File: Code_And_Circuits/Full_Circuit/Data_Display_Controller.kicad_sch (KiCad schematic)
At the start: 24 parts, among them M2 Stepper_Motor_bipolar, SW2 SW_Push_Dual_JST_XH_Input, U2 L293D, U5 TXB0104D, U6 74HC595

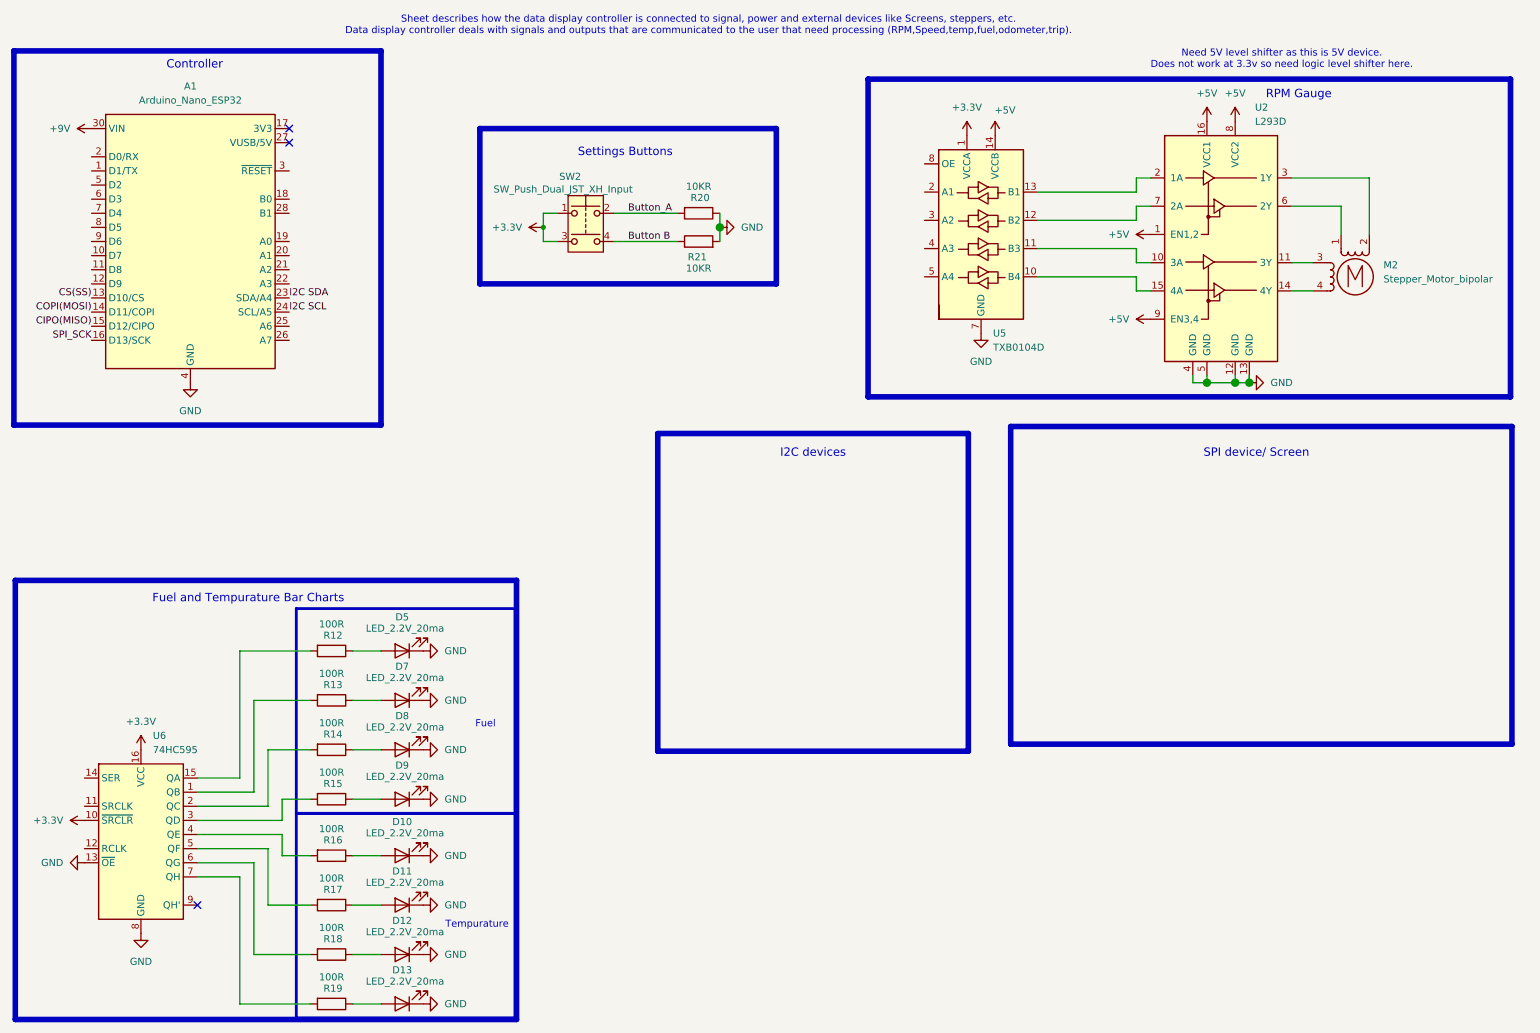
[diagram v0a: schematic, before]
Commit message: Finished schematic need to do PCB design and get Tachometer reference
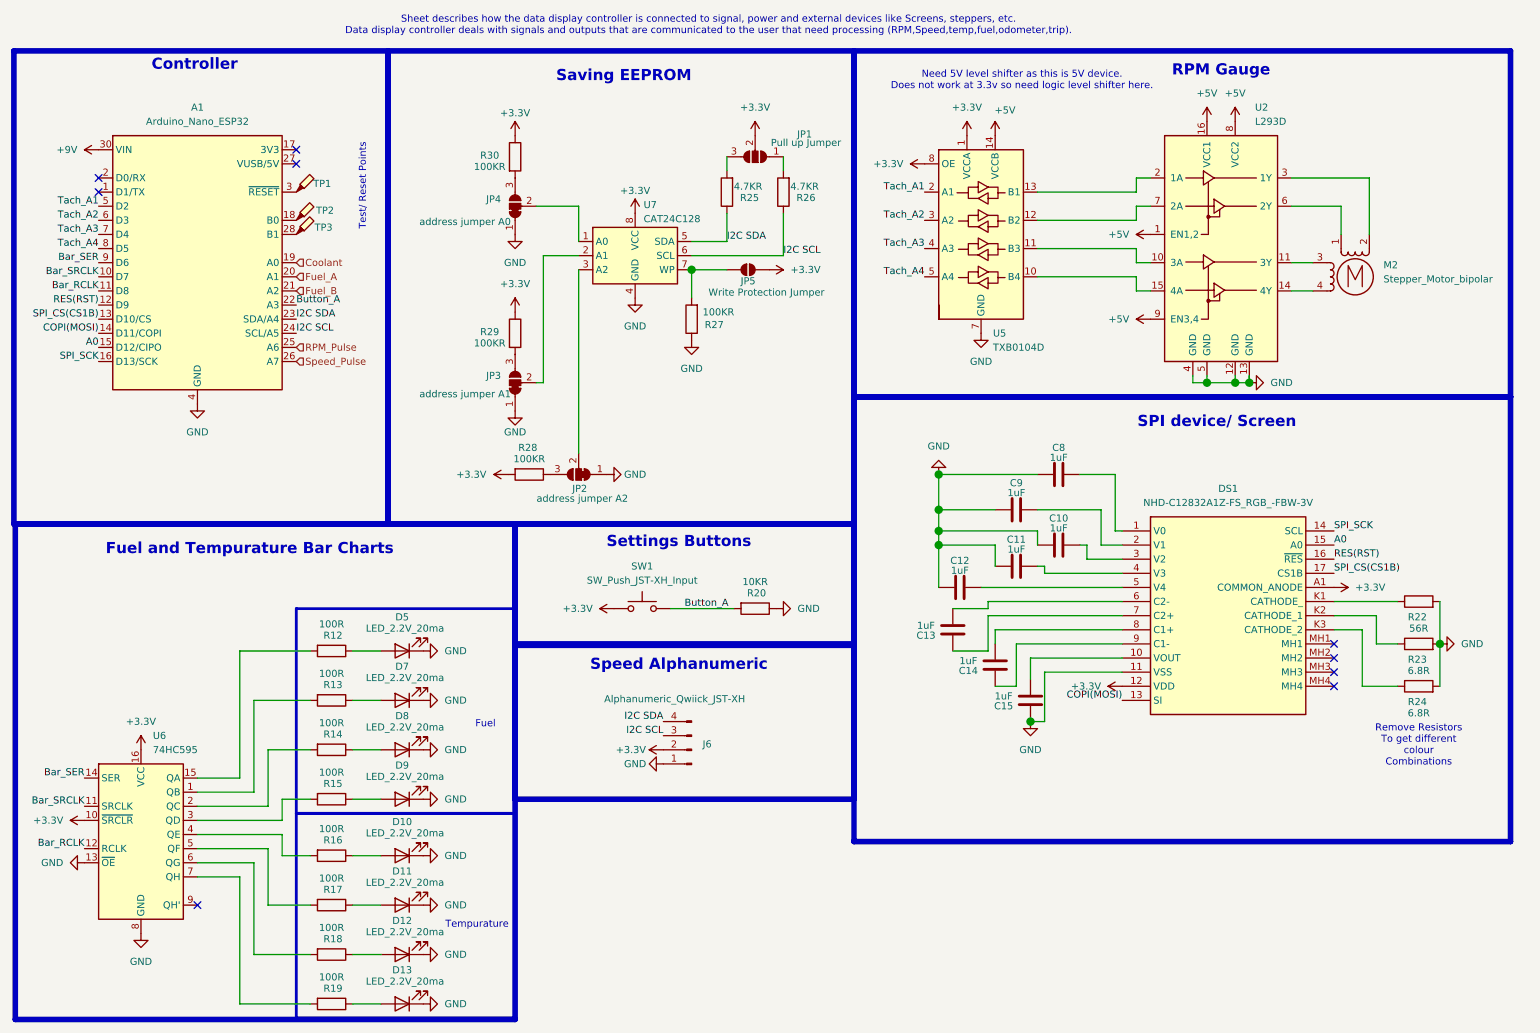
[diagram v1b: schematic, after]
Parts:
- removed R21: 10KR, Resistor_THT:R_Axial_DIN0204_L3.6mm_D1.6mm_P7.62mm_Horizontal, symbol Device:R
- removed SW2: SW_Push_Dual_JST_XH_Input, Connector_JST:JST_XH_B4B-XH-A_1x04_P2.50mm_Vertical, symbol Switch:SW_Push_Dual
- added C10, C11, C12, C13, C14, C15, C8, C9: 1uF, Capacitor_SMD:C_0805_2012Metric_Pad1.18x1.45mm_HandSolder, symbol Device:C
- added DS1: NHD-C12832A1Z-FS_RGB_-FBW-3V, Added_Footprints:NHDC12832A1ZFSRGBFBW3V, symbol Added_Symbols:NHD-C12832A1Z-FS_RGB_-FBW-3V
- added J6: Alphanumeric_Qwiick_JST-XH, symbol Connector:Conn_01x04_Pin
- added JP1: Pull up Jumper, Jumper:SolderJumper-3_P1.3mm_Open_RoundedPad1.0x1.5mm_NumberLabels, symbol Jumper:SolderJumper_3_Open
- added JP2: address jumper A2, Jumper:SolderJumper-3_P1.3mm_Bridged12_RoundedPad1.0x1.5mm_NumberLabels, symbol Jumper:SolderJumper_3_Bridged12
- added JP3: address jumper A1, Jumper:SolderJumper-3_P1.3mm_Bridged12_RoundedPad1.0x1.5mm_NumberLabels, symbol Jumper:SolderJumper_3_Bridged12
- added JP4: address jumper A0, Jumper:SolderJumper-3_P1.3mm_Bridged12_RoundedPad1.0x1.5mm_NumberLabels, symbol Jumper:SolderJumper_3_Bridged12
- added JP5: Write Protection Jumper, Jumper:SolderJumper-2_P1.3mm_Open_RoundedPad1.0x1.5mm, symbol Jumper:SolderJumper_2_Open
- added R22: 56R, Resistor_SMD:R_0805_2012Metric_Pad1.20x1.40mm_HandSolder, symbol Device:R
- added R23, R24: 6.8R, Resistor_SMD:R_0805_2012Metric_Pad1.20x1.40mm_HandSolder, symbol Device:R
- added R25, R26: 4.7KR, Resistor_SMD:R_0805_2012Metric_Pad1.20x1.40mm_HandSolder, symbol Device:R
- added R27, R28, R29, R30: 100KR, Resistor_SMD:R_0805_2012Metric_Pad1.20x1.40mm_HandSolder, symbol Device:R
- added SW1: SW_Push_JST-XH_Input, symbol Switch:SW_Push
- added TP1, TP2, TP3: TestPoint, Connector_PinHeader_1.00mm:PinHeader_1x01_P1.00mm_Vertical, symbol Connector:TestPoint_Probe
- added U7: CAT24C128, Package_SO:SOIC-8_3.9x4.9mm_P1.27mm, symbol Memory_EEPROM:CAT24C128
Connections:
- net +3.3V: now also U5.8 (OE), DS1.12 (VDD), DS1.A1 (COMMON_ANODE), J6.2 (Pin_2), JP1.2 (C), JP5.1 (A), R28.2, R29.1, R30.1, SW1.1, U7.8 (VCC)
- net Button_A: now also A1.22 (A3), SW1.2
- net COPI(MOSI): now also DS1.13 (SI)
- net GND: now also C10.1, C11.1, C12.1, C15.1, C8.1, C9.1, DS1.11 (VSS), J6.1 (Pin_1), JP2.1 (A), JP3.1 (A), JP4.1 (A), R22.2, R23.2, R24.2, R27.1, U7.4 (GND)
- net I2C SCL: now also J6.3 (Pin_3), R26.1, U7.6 (SCL)
- net I2C SDA: now also J6.4 (Pin_4), R25.1, U7.5 (SDA)
- net SPI_SCK: now also DS1.14 (SCL)
- net Bar_SRCLK: now reaches A1.10 (D7)
- net Bar_SRCLK: now also U6.11 (SRCLK)
- net Bar_RCLK: now reaches A1.11 (D8)
- net Bar_RCLK: now also U6.12 (RCLK)
- net RES(RST): now reaches A1.12 (D9)
- net RES(RST): now also DS1.16 (~{RES})
- net at A1.18 (B0): now also TP2.1
- net Coolant: now reaches A1.19 (A0)
- net Fuel_A: now reaches A1.20 (A1)
- net Fuel_B: now reaches A1.21 (A2)
- net RPM_Pulse: now reaches A1.25 (A6)
- net Speed_Pulse: now reaches A1.26 (A7)
- net at A1.28 (B1): now also TP3.1
- net at A1.3 (~{RESET}): now also TP1.1
- net Tach_A1: now reaches A1.5 (D2)
- net Tach_A1: now also U5.2 (A1)
- net Tach_A2: now reaches A1.6 (D3)
- net Tach_A2: now also U5.3 (A2)
- net Tach_A3: now reaches A1.7 (D4)
- net Tach_A3: now also U5.4 (A3)
- net Tach_A4: now reaches A1.8 (D5)
- net Tach_A4: now also U5.5 (A4)
- net Bar_SER: now reaches A1.9 (D6)
- net Bar_SER: now also U6.14 (SER)
- net CIPO(MISO) renamed A0
- net A0: now also DS1.15 (A0)
- net CS(SS) renamed SPI_CS(CS1B)
- net SPI_CS(CS1B): now also DS1.17 (CS1B)
- new net: C10.2, DS1.3 (V2)
- new net: JP1.1 (A), R26.2
- new net: C8.2, DS1.1 (V0)
- new net: JP4.3 (B), R30.2
- new net: C12.2, DS1.5 (V4)
- new net: JP1.3 (B), R25.2
- new net: C9.2, DS1.2 (V1)
- new net: JP4.2 (C), U7.1 (A0)
- new net: JP3.2 (C), U7.2 (A1)
- new net: JP2.2 (C), U7.3 (A2)
- new net: JP5.2 (B), R27.2, U7.7 (WP)
- new net: C11.2, DS1.4 (V3)
- new net: JP2.3 (B), R28.1
- new net: DS1.K2 (CATHODE_1), R23.1
- new net: JP3.3 (B), R29.2
- new net: DS1.K1 (CATHODE_), R22.1
- new net: DS1.K3 (CATHODE_2), R24.1
- new net: C15.2, DS1.10 (VOUT)
- new net: C13.2, DS1.6 (C2-)
- new net: C13.1, DS1.7 (C2+)
- new net: C14.2, DS1.8 (C1+)
- new net: C14.1, DS1.9 (C1-)
- no-connect marks 3 -> 9
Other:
- note added: "Remove Resistors To get different colour Combinations"
- note added: "Saving EEPROM"
- note added: "Speed Alphanumeric"
- note added: "Test/ Reset Points"
- note removed: "I2C devices"
- moved on the sheet: A1, R20

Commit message: Reconfired some pin assignments for cleaner layout and adding reference footprints and mostly layed out board, due to space limits logging section has been ommitted
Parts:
- added C19: 0.1 uF, Capacitor_SMD:C_0805_2012Metric_Pad1.18x1.45mm_HandSolder, symbol Device:C
- J6: footprint (none) -> Connector_JST:JST_XH_B4B-XH-A_1x04_P2.50mm_Vertical
- JP2, JP3, JP4, JP5, R27, R28, R29, R30: now not fitted
- M2: footprint (none) -> Added_Footprints:X27-168
- R12, R13, R14, R15, R16, R17, R18, R19: footprint Resistor_THT:R_Axial_DIN0204_L3.6mm_D1.6mm_P7.62mm_Horizontal -> Resistor_SMD:R_0805_2012Metric_Pad1.20x1.40mm_HandSolder
- SW1: footprint (none) -> Connector_JST:JST_XH_B2B-XH-A_1x02_P2.50mm_Vertical
- U6: footprint (none) -> Package_DIP:DIP-16_W7.62mm_Socket
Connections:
- net +9V: now also C19.1
- net Bar_RCLK: now also A1.10 (D7); no longer A1.11 (D8)
- net Bar_SRCLK: now also A1.11 (D8); no longer A1.10 (D7)
- net Coolant: now also A1.21 (A2); no longer A1.19 (A0)
- net Fuel_A: now also A1.19 (A0); no longer A1.20 (A1)
- net Fuel_B: now also A1.20 (A1); no longer A1.21 (A2)
- net GND: now also JP2.2 (C), JP3.2 (C), JP4.2 (C), JP5.2 (B), R27.2, U7.1 (A0), U7.2 (A1), U7.3 (A2), U7.7 (WP), C19.2
- net Tach_A1: now also A1.8 (D5); no longer A1.5 (D2)
- net Tach_A2: now also A1.7 (D4); no longer A1.6 (D3)
- net Tach_A3: now also A1.6 (D3); no longer A1.7 (D4)
- net Tach_A4: now also A1.5 (D2); no longer A1.8 (D5)
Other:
- note added: "decoulple cap"

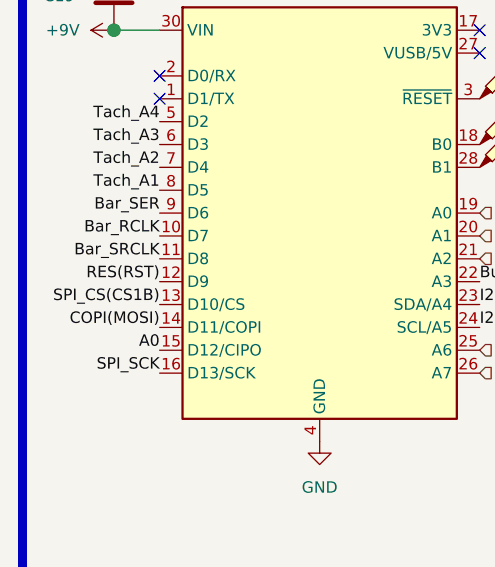
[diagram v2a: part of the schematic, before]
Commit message: Finished PCB layout for version 1
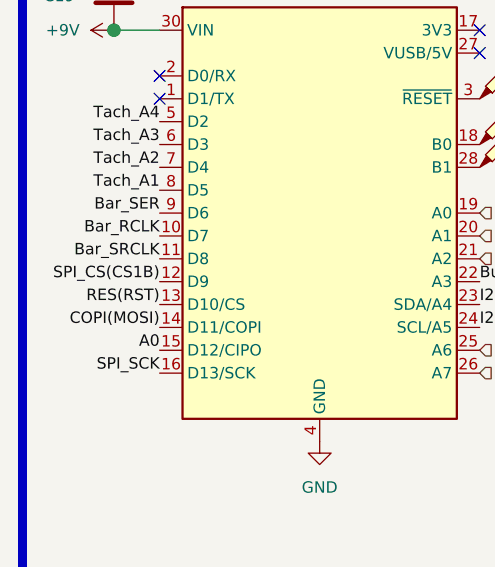
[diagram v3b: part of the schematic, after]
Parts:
- TP1, TP2, TP3: footprint Connector_PinHeader_1.00mm:PinHeader_1x01_P1.00mm_Vertical -> Connector_PinHeader_2.54mm:PinHeader_1x01_P2.54mm_Vertical
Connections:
- net RES(RST): now also A1.13 (D10/CS); no longer A1.12 (D9)
- net SPI_CS(CS1B): now also A1.12 (D9); no longer A1.13 (D10/CS)
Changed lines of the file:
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@@
 	)
 	(label "SPI_CS(CS1B)"
-		(at 29.21 69.85 180)
+		(at 29.21 67.31 180)
 		(effects
 			(font
@@
 	)
 	(label "RES(RST)"
-		(at 29.21 67.31 180)
+		(at 29.21 69.85 180)
 		(effects
 			(font
@@
 	)
 	(symbol
+		(lib_id "power:+3.3V")
+		(at 251.46 118.11 270)
+		(unit 1)
+		(exclude_from_sim no)
+		(in_bom yes)
+		(on_board yes)
+		(dnp no)
+		(fields_autoplaced yes)
+		(property "Reference" "#PWR052"
+			(at 247.65 118.11 0)
+			(effects
+				(font
+					(size 1.27 1.27)
+				)
+				(hide yes)
+			)
+		)
+		(property "Value" "+3.3V"
+			(at 255.27 118.1099 90)
+			(effects
+				(font
+					(size 1.27 1.27)
+				)
+				(justify left)
+			)
+		)
+		(property "Footprint" ""
+			(at 251.46 118.11 0)
+			(effects
+				(font
+					(size 1.27 1.27)
+				)
+				(hide yes)
+			)
+		)
+		(property "Datasheet" ""
+			(at 251.46 118.11 0)
+			(effects
+				(font
+					(size 1.27 1.27)
+				)
+				(hide yes)
+			)
+		)
+		(property "Description" "Power symbol creates a global label with name \"+3.3V\""
+			(at 251.46 118.11 0)
+			(effects
+				(font
+					(size 1.27 1.27)
+				)
+				(hide yes)
+			)
+		)
+		(pin "1"
+		)
+		(instances
+			(project "Full_Circuit"
+				(path "/619a717f-b37a-4dd9-96af-345e6fd91ffe/5c5ebc8e-da13-4330-b943-b878a884f7bc"
+					(reference "#PWR052")
+					(unit 1)
+				)
+			)
+		)
+	)
+	(symbol
 		(lib_id "power:GND")
 		(at 87.63 193.04 90)
@@
 				(path "/619a717f-b37a-4dd9-96af-345e6fd91ffe/5c5ebc8e-da13-4330-b943-b878a884f7bc"
 					(reference "R26")
-					(unit 1)
-				)
-			)
-		)
-	)
-	(symbol
-		(lib_id "power:+3.3V")
-		(at 251.46 118.11 270)
-		(unit 1)
-		(exclude_from_sim no)
-		(in_bom yes)
-		(on_board yes)
-		(dnp no)
-		(fields_autoplaced yes)
-		(property "Reference" "#PWR052"
-			(at 247.65 118.11 0)
-			(effects
-				(font
-					(size 1.27 1.27)
-				)
-				(hide yes)
-			)
-		)
-		(property "Value" "+3.3V"
-			(at 255.27 118.1099 90)
-			(effects
-				(font
-					(size 1.27 1.27)
-				)
-				(justify left)
-			)
-		)
-		(property "Footprint" ""
-			(at 251.46 118.11 0)
-			(effects
-				(font
-					(size 1.27 1.27)
-				)
-				(hide yes)
-			)
-		)
-		(property "Datasheet" ""
-			(at 251.46 118.11 0)
-			(effects
-				(font
-					(size 1.27 1.27)
-				)
-				(hide yes)
-			)
-		)
-		(property "Description" "Power symbol creates a global label with name \"+3.3V\""
-			(at 251.46 118.11 0)
-			(effects
-				(font
-					(size 1.27 1.27)
-				)
-				(hide yes)
-			)
-		)
-		(pin "1"
-		)
-		(instances
-			(project ""
-				(path "/619a717f-b37a-4dd9-96af-345e6fd91ffe/5c5ebc8e-da13-4330-b943-b878a884f7bc"
-					(reference "#PWR052")
 					(unit 1)
 				)
@@
 			)
 		)
-		(property "Footprint" "Connector_PinHeader_1.00mm:PinHeader_1x01_P1.00mm_Vertical"
+		(property "Footprint" "Connector_PinHeader_2.54mm:PinHeader_1x01_P2.54mm_Vertical"
 			(at 69.85 46.99 0)
 			(effects
@@
 			)
 		)
-		(property "Footprint" "Connector_PinHeader_1.00mm:PinHeader_1x01_P1.00mm_Vertical"
+		(property "Footprint" "Connector_PinHeader_2.54mm:PinHeader_1x01_P2.54mm_Vertical"
 			(at 69.85 52.07 0)
 			(effects
@@
 			)
 		)
-		(property "Footprint" "Connector_PinHeader_1.00mm:PinHeader_1x01_P1.00mm_Vertical"
+		(property "Footprint" "Connector_PinHeader_2.54mm:PinHeader_1x01_P2.54mm_Vertical"
 			(at 69.85 54.61 0)
 			(effects
